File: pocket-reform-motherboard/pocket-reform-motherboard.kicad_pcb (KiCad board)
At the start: 2 copper layers, 130 x 80 mm, 20 parts, among them J1 PWR, J2 Micro_SD_Card_Det, J3 USB_C_Receptacle, J4 AudioJack4, J5 USB_C_Receptacle, J6 USBINT, J7 HDMI_D_1.4, J8 SIM, U1 reform2-som-connector, U2 MPCIE-Socket-reform-motherboa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, U3 TUSB4041I, U4 WM8960, U6 MPCIE-Socket-reform-motherboa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

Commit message: motherboard D-1 first schematic and placement
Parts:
- added BT1: V364, Battery:BatteryHolder_Keystone_2998_1x6.8mm, F.Cu at (77.0, 146.8)
- added C1: 0.1uF, Capacitor_SMD:C_0603_1608Metric, F.Cu at (86.0, 138.5)
- added C10: 1uF, Capacitor_SMD:C_0603_1608Metric, F.Cu at (89.0, 105.3)
- added C11: 10nF, Capacitor_SMD:C_0603_1608Metric, F.Cu at (119.3, 147.2)
- added C12: 10nF, Capacitor_SMD:C_0603_1608Metric, F.Cu at (137.8, 147.5)
- added C123: 47uF, Capacitor_SMD:C_0603_1608Metric, F.Cu at (190.2, 140.5)
- added C124: 47uF, Capacitor_SMD:C_0603_1608Metric, F.Cu at (148.2, 138.2)
- added C126: 47uF, Capacitor_SMD:C_0603_1608Metric, F.Cu at (148.2, 140.0)
- added C13: 12pF, Capacitor_SMD:C_0603_1608Metric, F.Cu at (167.0, 84.2)
- added C14: 68uF, Capacitor_SMD:C_0603_1608Metric, F.Cu at (101.2, 136.5)
- added C15: 330uF, Capacitor_SMD:C_0603_1608Metric, F.Cu at (111.2, 149.0)
- added C16: 330uF, Capacitor_SMD:C_0603_1608Metric, F.Cu at (129.5, 149.2)
- added C17: 10uF, Capacitor_SMD:C_0603_1608Metric, F.Cu at (161.8, 81.8)
- added C18: 10nF, Capacitor_SMD:C_0603_1608Metric, F.Cu at (113.8, 150.0)
- added C19: 10nF, Capacitor_SMD:C_0603_1608Metric, F.Cu at (132.2, 150.5)
- added C2: 4.7uF, Capacitor_SMD:C_0603_1608Metric, F.Cu at (111.0, 142.5)
- added C20: 1uF, Capacitor_SMD:C_0603_1608Metric, F.Cu at (90.8, 122.0)
- added C21: 18pF, Capacitor_SMD:C_0603_1608Metric, F.Cu at (177.6, 109.8)
- added C22: 27pF, Capacitor_SMD:C_0603_1608Metric, F.Cu at (84.8, 82.8)
- added C23: 18pF, Capacitor_SMD:C_0603_1608Metric, F.Cu at (173.3, 106.9)
- added C24: 27pF, Capacitor_SMD:C_0603_1608Metric, F.Cu at (82.1, 79.1)
- added C25: 0.1uF, Capacitor_SMD:C_0603_1608Metric, F.Cu at (75.2, 74.2)
- added C26: 1uF, Capacitor_SMD:C_0603_1608Metric, F.Cu at (68.2, 83.8)
- added C27: 0.1uF, Capacitor_SMD:C_0603_1608Metric, F.Cu at (71.6, 74.2)
- added C28: 0.1uF, Capacitor_SMD:C_0603_1608Metric, F.Cu at (68.2, 79.0)
- added C29: 0.1uF, Capacitor_SMD:C_0603_1608Metric, F.Cu at (80.8, 75.5)
- added C3: 4.7uF, Capacitor_SMD:C_0603_1608Metric, F.Cu at (129.5, 142.8)
- added C30: 0.1uF, Capacitor_SMD:C_0603_1608Metric, F.Cu at (80.8, 77.2)
- added C31: 0.1uF, Capacitor_SMD:C_0603_1608Metric, F.Cu at (75.2, 86.0)
- added C32: 0.1uF, Capacitor_SMD:C_0603_1608Metric, F.Cu at (71.2, 86.0)
- added C33: 0.1uF, Capacitor_SMD:C_0603_1608Metric, F.Cu at (68.2, 82.2)
- added C34: 1uF, Capacitor_SMD:C_0603_1608Metric, F.Cu at (68.2, 77.5)
- added C35: 0.1uF, Capacitor_SMD:C_0603_1608Metric, F.Cu at (62.0, 74.2)
- added C36: 1uF, Capacitor_SMD:C_0603_1608Metric, F.Cu at (68.2, 75.8)
- added C37: 1nF, Capacitor_SMD:C_0603_1608Metric, F.Cu at (195.5, 69.0)
- added C38: 0.1uF, Capacitor_SMD:C_0603_1608Metric, F.Cu at (80.8, 73.9)
- added C39: 10uF, Capacitor_SMD:C_0603_1608Metric, F.Cu at (170.5, 78.0)
- added C4: 4.7uF, Capacitor_SMD:C_0603_1608Metric, F.Cu at (112.8, 142.5)
- added C40: 0.1uF, Capacitor_SMD:C_0603_1608Metric, F.Cu at (68.2, 80.8)
- added C41: 0.1uF, Capacitor_SMD:C_0603_1608Metric, F.Cu at (170.5, 79.8)
- added C42: 0.1uF, Capacitor_SMD:C_0603_1608Metric, F.Cu at (188.0, 69.0)
- added C43: 0.1uF, Capacitor_SMD:C_0603_1608Metric, F.Cu at (186.5, 69.0)
- added C44: 0.1uF, Capacitor_SMD:C_0603_1608Metric, F.Cu at (185.0, 69.0)
- added C45: 0.1uF, Capacitor_SMD:C_0603_1608Metric, F.Cu at (183.5, 69.0)
- added C46: 0.1uF, Capacitor_SMD:C_0603_1608Metric, F.Cu at (80.5, 98.5)
- added C47: 0.1uF, Capacitor_SMD:C_0603_1608Metric, F.Cu at (197.0, 133.2)
- added C48: 0.1uF, Capacitor_SMD:C_0603_1608Metric, F.Cu at (159.0, 122.8)
- added C49: 0.1uF, Capacitor_SMD:C_0603_1608Metric, F.Cu at (157.9, 112.0)
- added C5: 4.7uF, Capacitor_SMD:C_0603_1608Metric, F.Cu at (131.2, 142.8)
- added C50: 0.1uF, Capacitor_SMD:C_0603_1608Metric, F.Cu at (77.5, 128.2)
- added C51: 10uF, Capacitor_SMD:C_0603_1608Metric, F.Cu at (80.7, 126.5)
- added C52: 10nF, Capacitor_SMD:C_0603_1608Metric, F.Cu at (171.2, 137.6)
- added C53: 0.1uF, Capacitor_SMD:C_0603_1608Metric, F.Cu at (171.2, 140.6)
- added C54: 0.1uF, Capacitor_SMD:C_0603_1608Metric, F.Cu at (171.2, 139.0)
- added C55: 0.1uF, Capacitor_SMD:C_0603_1608Metric, F.Cu at (175.8, 140.5)
- added C56: 10uF, Capacitor_SMD:C_0603_1608Metric, F.Cu at (69.5, 122.0)
- added C57: 0.1uF, Capacitor_SMD:C_0603_1608Metric, F.Cu at (80.5, 121.5)
- added C58: 10nF, Capacitor_SMD:C_0603_1608Metric, F.Cu at (159.0, 138.5)
- added C59: 0.1uF, Capacitor_SMD:C_0603_1608Metric, F.Cu at (162.2, 138.5)
- added C6: 4.7uF, Capacitor_SMD:C_0603_1608Metric, F.Cu at (163.0, 91.2)
- added C60: 0.1uF, Capacitor_SMD:C_0603_1608Metric, F.Cu at (162.2, 140.2)
- added C61: 0.1uF, Capacitor_SMD:C_0603_1608Metric, F.Cu at (165.5, 140.2)
- added C62: 0.1uF, Capacitor_SMD:C_0603_1608Metric, F.Cu at (71.0, 122.1)
- added C63: 0.1uF, Capacitor_SMD:C_0603_1608Metric, F.Cu at (163.2, 111.0)
- added C64: 0.1uF, Capacitor_SMD:C_0603_1608Metric, F.Cu at (162.2, 122.8)
- added C65: 10uF, Capacitor_SMD:C_0603_1608Metric, F.Cu at (191.2, 105.8)
- added C66: 0.1uF, Capacitor_SMD:C_0603_1608Metric, F.Cu at (193.0, 105.8)
- added C67: 10uF, Capacitor_SMD:C_0603_1608Metric, F.Cu at (80.0, 124.0)
- added C68: 0.1uF, Capacitor_SMD:C_0603_1608Metric, F.Cu at (74.5, 130.0)
- added C69: 0.1uF, Capacitor_SMD:C_0603_1608Metric, F.Cu at (80.0, 117.0)
- added C7: 10nF, Capacitor_SMD:C_0603_1608Metric, F.Cu at (114.5, 142.5)
- added C72: 0.1uF, Capacitor_SMD:C_0603_1608Metric, F.Cu at (199.3, 90.1)
- added C73: 0.1uF, Capacitor_SMD:C_0603_1608Metric, F.Cu at (193.0, 88.5)
- added C76: 0.1uF, Capacitor_SMD:C_0603_1608Metric, F.Cu at (69.7, 138.1)
- added C77: 0.1uF, Capacitor_SMD:C_0603_1608Metric, F.Cu at (186.8, 88.0)
- added C78: 0.1uF, Capacitor_SMD:C_0603_1608Metric, F.Cu at (65.0, 148.5)
- added C8: 10nF, Capacitor_SMD:C_0603_1608Metric, F.Cu at (133.0, 142.8)
- added C82: 470nF, Capacitor_SMD:C_0603_1608Metric, F.Cu at (68.5, 146.0)
- added C83: 47uF, Capacitor_SMD:C_0603_1608Metric, F.Cu at (187.2, 140.5)
- added C85: 0.1uF, Capacitor_SMD:C_0603_1608Metric, F.Cu at (170.2, 119.2)
- added C86: 0.1uF, Capacitor_SMD:C_0603_1608Metric, F.Cu at (170.2, 125.8)
- added C87: 0.1uF, Capacitor_SMD:C_0603_1608Metric, F.Cu at (200.2, 98.9)
- added C88: 0.1uF, Capacitor_SMD:C_0603_1608Metric, F.Cu at (168.8, 119.2)
- added C89: 0.1uF, Capacitor_SMD:C_0603_1608Metric, F.Cu at (168.8, 125.8)
- added C9: 1uF, Capacitor_SMD:C_0603_1608Metric, F.Cu at (93.4, 105.2)
- added C90: 0.1uF, Capacitor_SMD:C_0603_1608Metric, F.Cu at (178.8, 129.0)
- added C91: 0.1uF, Capacitor_SMD:C_0603_1608Metric, F.Cu at (182.5, 129.0)
- added C92: 0.1uF, Capacitor_SMD:C_0603_1608Metric, F.Cu at (177.2, 129.0)
- added C93: 0.1uF, Capacitor_SMD:C_0603_1608Metric, F.Cu at (181.0, 129.0)
- added D1: LED_MODEM, LED_SMD:LED_0603_1608Metric, F.Cu at (193.6, 149.5)
- added D10: 19-337/R6GHBHC-A01/2T, LED_SMD:LED_RGB_PLCC-6, F.Cu at (67.5, 70.1)
- added D11: SS54?, Diode_SMD:D_SMA, F.Cu at (91.8, 138.0)
- added D12: SD0603S040S0R2, Diode_SMD:D_0603_1608Metric, F.Cu at (189.8, 88.5)
- added D2: SMAJ36CA-E3/5A, Diode_SMD:D_SMA, F.Cu at (78.6, 139.8)
- added D23: LED_NVME, LED_SMD:LED_0603_1608Metric, F.Cu at (168.1, 149.5)
- added D3: BZT52C10, Diode_SMD:D_SOD-123, F.Cu at (85.5, 140.5)
- added D4: B540C, Diode_SMD:D_SMA, F.Cu at (102.8, 140.0)
- added D5: B540C, Diode_SMD:D_SMA, F.Cu at (108.5, 147.8)
- added D6: B540C, Diode_SMD:D_SMA, F.Cu at (126.8, 147.8)
- added D7: BZX84-C5V6,215, Diode_SMD:D_SOD-323, F.Cu at (88.8, 122.2)
- added D8: LED_Small, LED_SMD:LED_0603_1608Metric, F.Cu at (201.5, 68.2)
- added D9: LED_Small, LED_SMD:LED_0603_1608Metric, F.Cu at (201.5, 70.0)
- added FB1: 220@100MHz 1.4A, Inductor_SMD:L_0603_1608Metric, F.Cu at (170.5, 81.5)
- added FB10: 100@100MHz 3A, Inductor_SMD:L_0603_1608Metric, F.Cu at (73.0, 139.5)
- added FB2: 100@100MHz 3A, Inductor_SMD:L_0603_1608Metric, F.Cu at (80.5, 119.8)
- added FB3: 100@100MHz 3A, Inductor_SMD:L_0603_1608Metric, F.Cu at (171.3, 135.9)
- added FB4: 100@100MHz 3A, Inductor_SMD:L_0603_1608Metric, F.Cu at (146.5, 136.6)
- added FB5: 100@100MHz 3A, Inductor_SMD:L_0603_1608Metric, F.Cu at (76.9, 117.0)
- added FB8: 100@100MHz 3A, Inductor_SMD:L_0603_1608Metric, F.Cu at (164.8, 111.0)
- added FB9: 100@100MHz 3A, Inductor_SMD:L_0603_1608Metric, F.Cu at (71.5, 139.5)
- added H5: NGFF-Mount1, footprints:WA-SMSI-M2, F.Cu at (156.0, 87.0)
- added H6: NGFF-Mount1, footprints:WA-SMSI-M2, F.Cu at (156.0, 107.0)
- added H7: NGFF-Mount1, footprints:WA-SMSI-M2, F.Cu at (181.0, 107.0)
- added J10: 1-2199230-6, footprints:TE_1-2199230-6, F.Cu at (156.0, 145.0)
- added J11: Conn_01x33, Connector_FFC-FPC:Hirose_FH12-33S-0.5SH_1x33-1MP_P0.50mm_Horizontal, F.Cu at (64.8, 116.6)
- added J12: 2199230-5, footprints:TE_2199230-5, F.Cu at (181.0, 145.0)
- added J13: FH35C-31S-0.3HW(50), footprints:TE_3-2328724-1, F.Cu at (61.9, 133.8)
- added J14: USB_C_Receptacle, Connector_USB:USB_C_Receptacle_Amphenol_12401548E4-2A_CircularHoles, F.Cu at (204.9, 141.0)
- added J15: Conn_01x02, Connector_JST:JST_GH_SM02B-GHS-TB_1x02-1MP_P1.25mm_Horizontal, F.Cu at (63.3, 143.2)
- added J9: USB_C_Receptacle_USB2.0, Connector_USB:USB_C_Receptacle_HRO_TYPE-C-31-M-12, F.Cu at (148.7, 71.1)
- added L1: 47uH, Inductor_SMD:L_1210_3225Metric, F.Cu at (96.5, 140.0)
- added L2: 2.2uH, Inductor_SMD:L_1210_3225Metric, F.Cu at (162.0, 84.2)
- added L3: 15uH, Inductor_SMD:L_1210_3225Metric, F.Cu at (113.8, 146.8)
- added L4: 15uH, Inductor_SMD:L_1210_3225Metric, F.Cu at (132.2, 147.3)
- added L5: 15uH, Inductor_SMD:L_1210_3225Metric, F.Cu at (68.6, 142.3)
- added L6: 15uH, Inductor_SMD:L_1210_3225Metric, F.Cu at (68.3, 148.7)
- added MK1: MP23ABS1TR, footprints:MIC_MP23ABS1TR, F.Cu at (97.7, 68.9)
- added Q1: Si7461DP, footprints:PowerPAK_SO-8_Single_8Pads, F.Cu at (85.2, 133.8)
- added R1: 1k, Resistor_SMD:R_0603_1608Metric, F.Cu at (195.5, 149.5)
- added R10: 200k, Resistor_SMD:R_0603_1608Metric, F.Cu at (167.8, 87.8)
- added R100: 47k, Resistor_SMD:R_0603_1608Metric, F.Cu at (116.1, 70.0)
- added R101: 0, Resistor_SMD:R_0603_1608Metric, F.Cu at (181.6, 137.2)
- added R102: 0, Resistor_SMD:R_0603_1608Metric, F.Cu at (181.6, 135.7)
- added R103: 0, Resistor_SMD:R_0603_1608Metric, F.Cu at (187.2, 138.5)
- added R104: 0, Resistor_SMD:R_0603_1608Metric, F.Cu at (161.7, 134.5)
- added R105: 0, Resistor_SMD:R_0603_1608Metric, F.Cu at (158.1, 134.5)
- added R106: 0, Resistor_SMD:R_0603_1608Metric, F.Cu at (154.6, 134.5)
- added R107: 0, Resistor_SMD:R_0603_1608Metric, F.Cu at (163.2, 134.5)
- added R108: 0, Resistor_SMD:R_0603_1608Metric, F.Cu at (159.6, 134.5)
- added R109: 0, Resistor_SMD:R_0603_1608Metric, F.Cu at (156.1, 134.5)
- added R11: 0, Resistor_SMD:R_0603_1608Metric, F.Cu at (126.4, 96.9)
- added R110: 1k, Resistor_SMD:R_0603_1608Metric, F.Cu at (168.1, 143.5)
- added R111: 0, Resistor_SMD:R_0603_1608Metric, F.Cu at (190.2, 138.5)
- added R12: 0, Resistor_SMD:R_0603_1608Metric, F.Cu at (87.8, 82.3)
- added R13: 0, Resistor_SMD:R_0603_1608Metric, F.Cu at (87.8, 84.0)
- added R14: 280k, Resistor_SMD:R_0603_1608Metric, F.Cu at (165.5, 84.2)
- added R15: 10k, Resistor_SMD:R_0603_1608Metric, F.Cu at (124.0, 145.5)
- added R16: 3.16k, Resistor_SMD:R_0603_1608Metric, F.Cu at (124.0, 142.2)
- added R17: 10k, Resistor_SMD:R_0603_1608Metric, F.Cu at (142.5, 145.4)
- added R18: 5.83k, Resistor_SMD:R_0603_1608Metric, F.Cu at (142.5, 142.1)
- added R19: 1.3M, Resistor_SMD:R_0603_1608Metric, F.Cu at (97.2, 122.8)
- added R198: 49.9, Resistor_SMD:R_0603_1608Metric, F.Cu at (126.8, 116.0)
- added R199: 49.9, Resistor_SMD:R_0603_1608Metric, F.Cu at (126.8, 114.5)
- added R2: 62, Resistor_SMD:R_0603_1608Metric, F.Cu at (80.7, 136.7)
- added R20: 300k, Resistor_SMD:R_0603_1608Metric, F.Cu at (98.9, 122.9)
- added R21: 1M, Resistor_SMD:R_0603_1608Metric, F.Cu at (90.8, 125.2)
- added R22: 10k, Resistor_SMD:R_0603_1608Metric, F.Cu at (172.5, 129.0)
- added R23: DNP, Resistor_SMD:R_0603_1608Metric, F.Cu at (174.0, 129.0)
- added R24: 4.7k, Resistor_SMD:R_0603_1608Metric, F.Cu at (187.0, 120.2)
- added R25: 4.7k, Resistor_SMD:R_0603_1608Metric, F.Cu at (187.8, 122.8)
- added R26: 4.7k, Resistor_SMD:R_0603_1608Metric, F.Cu at (188.8, 120.2)
- added R27: 200k, Resistor_SMD:R_0603_1608Metric, F.Cu at (175.5, 129.0)
- added R28: 120k, Resistor_SMD:R_0603_1608Metric, F.Cu at (93.5, 125.5)
- added R29: 1k, Resistor_SMD:R_0603_1608Metric, F.Cu at (198.2, 68.3)
- added R3: 1M, Resistor_SMD:R_0603_1608Metric, F.Cu at (89.0, 136.0)
- added R30: 10k, Resistor_SMD:R_0603_1608Metric, F.Cu at (186.0, 110.2)
- added R31: 36k, Resistor_SMD:R_0603_1608Metric, F.Cu at (186.0, 107.2)
- added R32: 10k, Resistor_SMD:R_0603_1608Metric, F.Cu at (186.0, 108.8)
- added R33: 36k, Resistor_SMD:R_0603_1608Metric, F.Cu at (186.0, 105.8)
- added R34: 1k, Resistor_SMD:R_0603_1608Metric, F.Cu at (198.2, 70.0)
- added R35: 1k, Resistor_SMD:R_0603_1608Metric, F.Cu at (79.6, 80.7)
- added R36: 1k, Resistor_SMD:R_0603_1608Metric, F.Cu at (63.1, 86.3)
- added R37: 75 1%, Resistor_SMD:R_0603_1608Metric, F.Cu at (189.5, 69.0)
- added R38: 10k, Resistor_SMD:R_0603_1608Metric, F.Cu at (61.6, 86.4)
- added R39: 75 1%, Resistor_SMD:R_0603_1608Metric, F.Cu at (191.0, 69.0)
- added R4: 0, Resistor_SMD:R_0603_1608Metric, F.Cu at (96.0, 103.2)
- added R40: 75 1%, Resistor_SMD:R_0603_1608Metric, F.Cu at (192.5, 69.0)
- added R41: 75 1%, Resistor_SMD:R_0603_1608Metric, F.Cu at (194.0, 69.0)
- added R44: 0, Resistor_SMD:R_0603_1608Metric, F.Cu at (81.8, 86.2)
- added R45: 0, Resistor_SMD:R_0603_1608Metric, F.Cu at (86.8, 77.2)
- added R46: 0, Resistor_SMD:R_0603_1608Metric, F.Cu at (77.0, 90.2)
- added R47: 27.4, Resistor_SMD:R_0603_1608Metric, F.Cu at (92.1, 78.6)
- added R48: 27.4, Resistor_SMD:R_0603_1608Metric, F.Cu at (92.1, 80.2)
- added R49: 0, Resistor_SMD:R_0603_1608Metric, F.Cu at (77.0, 91.8)
- added R5: 0, Resistor_SMD:R_0603_1608Metric, F.Cu at (142.7, 88.1)
- added R50: 0, Resistor_SMD:R_0603_1608Metric, F.Cu at (81.8, 88.0)
- added R51: 0, Resistor_SMD:R_0603_1608Metric, F.Cu at (77.0, 93.2)
- added R52: 10k, Resistor_SMD:R_0603_1608Metric, F.Cu at (182.6, 111.3)
- added R53: 12k 1%, Resistor_SMD:R_0603_1608Metric, F.Cu at (170.8, 109.4)
- added R54: 10k, Resistor_SMD:R_0603_1608Metric, F.Cu at (170.8, 113.0)
- added R55: 200k, Resistor_SMD:R_0603_1608Metric, F.Cu at (187.0, 115.5)
- added R56: 10k, Resistor_SMD:R_0603_1608Metric, F.Cu at (65.0, 97.5)
- added R57: 4.7k, Resistor_SMD:R_0603_1608Metric, F.Cu at (69.2, 87.5)
- added R58: 1k, Resistor_SMD:R_0603_1608Metric, F.Cu at (71.8, 68.3)
- added R59: 4.7k, Resistor_SMD:R_0603_1608Metric, F.Cu at (67.5, 87.5)
- added R6: 100k, Resistor_SMD:R_0603_1608Metric, F.Cu at (117.0, 137.2)
- added R60: 1k, Resistor_SMD:R_0603_1608Metric, F.Cu at (71.9, 70.1)
- added R61: 1k, Resistor_SMD:R_0603_1608Metric, F.Cu at (71.9, 71.7)
- added R62: DNP, Resistor_SMD:R_0603_1608Metric, F.Cu at (152.1, 77.3)
- added R63: DNP, Resistor_SMD:R_0603_1608Metric, F.Cu at (147.5, 78.2)
- added R64: DNP, Resistor_SMD:R_0603_1608Metric, F.Cu at (149.2, 78.2)
- added R65: 49.9, Resistor_SMD:R_0603_1608Metric, F.Cu at (126.8, 111.5)
- added R66: 49.9, Resistor_SMD:R_0603_1608Metric, F.Cu at (126.8, 113.0)
- added R67: 0, Resistor_SMD:R_0603_1608Metric, F.Cu at (126.4, 89.8)
- added R68: 10k, Resistor_SMD:R_0603_1608Metric, F.Cu at (194.8, 130.8)
- added R69: 100k, Resistor_SMD:R_0603_1608Metric, F.Cu at (72.0, 115.0)
- added R7: 100k, Resistor_SMD:R_0603_1608Metric, F.Cu at (117.0, 135.5)
- added R70: 0, Resistor_SMD:R_0603_1608Metric, F.Cu at (73.0, 117.7)
- added R71: 0, Resistor_SMD:R_0603_1608Metric, F.Cu at (71.0, 125.5)
- added R72: 2k2, Resistor_SMD:R_0603_1608Metric, F.Cu at (74.5, 128.5)
- added R75: 10k, Resistor_SMD:R_0603_1608Metric, F.Cu at (164.8, 122.0)
- added R76: 33, Resistor_SMD:R_0603_1608Metric, F.Cu at (108.0, 119.7)
- added R77: 33, Resistor_SMD:R_0603_1608Metric, F.Cu at (106.3, 124.8)
- added R79: 33, Resistor_SMD:R_0603_1608Metric, F.Cu at (112.0, 123.2)
- added R8: 100k, Resistor_SMD:R_0603_1608Metric, F.Cu at (167.2, 90.2)
- added R80: 33, Resistor_SMD:R_0603_1608Metric, F.Cu at (126.6, 81.1)
- added R81: 0, Resistor_SMD:R_0603_1608Metric, F.Cu at (160.0, 110.2)
- added R82: 33, Resistor_SMD:R_0603_1608Metric, F.Cu at (126.5, 79.5)
- added R83: 0, Resistor_SMD:R_0603_1608Metric, F.Cu at (169.6, 123.2)
- added R84: 0, Resistor_SMD:R_0603_1608Metric, F.Cu at (169.6, 121.7)
- added R85: 10k, Resistor_SMD:R_0603_1608Metric, F.Cu at (187.8, 90.5)
- added R87: 100k, Resistor_SMD:R_0603_1608Metric, F.Cu at (126.7, 127.6)
- added R89: 4.7k, Resistor_SMD:R_0603_1608Metric, F.Cu at (201.8, 88.5)
- added R9: 0, Resistor_SMD:R_0603_1608Metric, F.Cu at (98.2, 133.0)
- added R90: 27k, Resistor_SMD:R_0603_1608Metric, F.Cu at (197.5, 87.8)
- added R93: 4.7k, Resistor_SMD:R_0603_1608Metric, F.Cu at (201.8, 87.0)
- added R96: 10k, Resistor_SMD:R_0603_1608Metric, F.Cu at (207.2, 87.8)
- added R97: 47k, Resistor_SMD:R_0603_1608Metric, F.Cu at (116.1, 68.5)
- added R98: 47k, Resistor_SMD:R_0603_1608Metric, F.Cu at (116.1, 71.5)
- added R99: 47k, Resistor_SMD:R_0603_1608Metric, F.Cu at (116.1, 72.9)
- added SW1: SW_DIP_x01, Button_Switch_SMD:SW_DIP_SPSTx01_Slide_Omron_A6S-110x_W8.9mm_P2.54mm, F.Cu at (61.4, 93.4)
- added SW2: RESET, Button_Switch_SMD:SW_Push_1P1T_NO_CK_KMR2, F.Cu at (61.2, 102.0)
- added TP3: PRTCTL2, TestPoint:TestPoint_Pad_D1.0mm, F.Cu at (188.8, 126.8)
- added TP4: PRTCTL4, TestPoint:TestPoint_Pad_D1.0mm, F.Cu at (186.6, 129.9)
- added TP5: TestPoint, TestPoint:TestPoint_Pad_D1.0mm, F.Cu at (80.1, 69.8)
- added TP6: TestPoint, TestPoint:TestPoint_Pad_D1.0mm, F.Cu at (82.8, 69.8)
- added TR1: TG111-MSC13LF, Transformer_SMD:Transformer_Ethernet_HALO_TG111-MSC13, F.Cu at (188.8, 78.4)
- added U10: W25Q32JVSS, Package_SO:SOIC-8_5.23x5.23mm_P1.27mm, F.Cu at (63.4, 80.0)
- added U11: PCF8523T, Package_SO:SOIC-8_3.9x4.9mm_P1.27mm, F.Cu at (75.8, 99.5)
- added U12: AP22815, Package_TO_SOT_SMD:SOT-23-5, F.Cu at (194.0, 133.3)
- added U13: TXS0108EPW, Package_SO:TSSOP-20_4.4x6.5mm_P0.65mm, F.Cu at (161.5, 116.5)
- added U14: SN74AVC1T45, Package_TO_SOT_SMD:SOT-23-6, F.Cu at (161.7, 125.5)
- added U15: TPD4E02B04DQA, Package_SON:USON-10_2.5x1.0mm_P0.5mm, F.Cu at (195.5, 141.2)
- added U16: TPD4E02B04DQA, Package_SON:USON-10_2.5x1.0mm_P0.5mm, F.Cu at (195.5, 124.0)
- added U17: TPD12S521, footprints:TSSOP50P640X120-38N, F.Cu at (193.7, 94.8)
- added U18: TLV320AIC3100, Package_DFN_QFN:VQFN-32-1EP_5x5mm_P0.5mm_EP3.5x3.5mm, F.Cu at (75.3, 123.3)
- added U19: TPD4E02B04DQA, Package_SON:USON-10_2.5x1.0mm_P0.5mm, F.Cu at (195.5, 144.5)
- added U20: TPD4E02B04DQA, Package_SON:USON-10_2.5x1.0mm_P0.5mm, F.Cu at (195.5, 127.5)
- added U21: TPD4E02B04DQA, Package_SON:USON-10_2.5x1.0mm_P0.5mm, F.Cu at (195.5, 138.0)
- added U22: TPD4E02B04DQA, Package_SON:USON-10_2.5x1.0mm_P0.5mm, F.Cu at (195.5, 120.5)
- added U23: FUSB302BMPX, Package_DFN_QFN:WQFN-14-1EP_2.5x2.5mm_P0.5mm_EP1.45x1.45mm, F.Cu at (149.5, 131.7)
- added U5: TPS5450DDAR, Package_SO:TI_SO-PowerPAD-8_ThermalVias, F.Cu at (119.2, 143.5)
- added U7: CN301, Package_TO_SOT_SMD:SOT-23-5, F.Cu at (94.0, 122.8)
- added U8: RP2040, footprints:RP2040-QFN-56, F.Cu at (74.4, 80.1)
- added U9: USB7002/KDX, footprints:QFN40P1200X1200X90-101N, F.Cu at (179.2, 119.4)
- added Y1: 25MHz, Crystal:Crystal_SMD_Abracon_ABM8G-4Pin_3.2x2.5mm, F.Cu at (174.5, 109.7)
- added Y2: 12MHz 18pF, Crystal:Crystal_SMD_3225-4Pin_3.2x2.5mm, F.Cu at (82.1, 82.2)
- added Y3: 32.768 kHz, Crystal:Crystal_SMD_3215-2Pin_3.2x1.5mm, F.Cu at (70.4, 98.8)
- J1: value PWR -> CHARGER; footprint Connector_JST:JST_PH_S4B-PH-SM4-TB_1x04-1MP_P2.00mm_Horizontal -> Connector_JST:JST_PH_S9B-PH-SM4-TB_1x09-1MP_P2.00mm_Horizontal
- J4: value AudioJack4 -> 09452812561; footprint Connector_Audio:Jack_3.5mm_CUI_SJ-3524-SMT_Horizontal -> footprints:09452812561
- J5: value USB_C_Receptacle -> SYSCTL; footprint Connector_USB:USB_C_Receptacle_Amphenol_12401548E4-2A_CircularHoles -> Connector_JST:JST_PH_S4B-PH-SM4-TB_1x04-1MP_P2.00mm_Horizontal
- J6: value USBINT -> USB_INT1
- J8: value SIM -> SIM_Card; footprint footprints:TE_2199337-5 -> footprints:MOLEX_78800-0001
- TP1: value TestPoint_2Pole -> PRTCTL1; footprint footprints:MOLEX_48099-5701 -> TestPoint:TestPoint_Pad_D1.0mm
- TP2: value TestPoint_2Pole -> PRTCTL3; footprint footprints:MOLEX_48099-5701 -> TestPoint:TestPoint_Pad_D1.0mm
- U2: value MPCIE-Socket-reform-motherboard-rescue -> MAX1837EUT33+T; footprint footprints:MOLEX_67910-5700 -> Package_TO_SOT_SMD:SOT-23-6
- U3: value TUSB4041I -> LM3674MFX-ADJ/NOPB; footprint Package_QFP:HTQFP-64-1EP_10x10mm_P0.5mm_EP8x8mm_Mask4.4x4.4mm_ThermalVias -> Package_TO_SOT_SMD:SOT-23-5
- U4: value WM8960 -> TLV1117-18; footprint Package_DFN_QFN:QFN-32-1EP_5x5mm_P0.5mm_EP3.3x3.3mm -> Package_TO_SOT_SMD:SOT-223
- U6: value MPCIE-Socket-reform-motherboard-rescue -> TPS5450DDAR; footprint footprints:MOLEX_67910-5700 -> Package_SO:TI_SO-PowerPAD-8_ThermalVias
- moved J2 97.5 mm to (201.5, 108.8), turned to 90 degrees
- moved U4 95.5 mm to (90.5, 99.8), turned to 90 degrees
- moved J1 70.5 mm to (94.8, 147.0), turned to 0 degrees
- moved J7 63.0 mm to (207.0, 94.8), turned to 90 degrees
- moved U2 62.6 mm to (98.7, 136.0), turned to -90 degrees
- moved J3 52.1 mm to (205.0, 124.0), turned to 90 degrees
- moved J8 49.6 mm to (177.5, 95.0), turned to -90 degrees
- moved GFX1 33.9 mm to (146.8, 106.8), turned to 90 degrees
- moved TP2 29.6 mm to (188.7, 128.9), turned to 0 degrees
- moved H1 20.6 mm to (62.0, 70.0)
- moved H2 20.0 mm to (62.0, 149.0)
- moved TP1 18.5 mm to (186.7, 127.7), turned to 0 degrees
- moved J6 16.6 mm to (174.5, 72.0)
- moved U6 16.5 mm to (137.8, 143.8), turned to 180 degrees
- moved U1 13.3 mm to (135.0, 104.0)
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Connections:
- net Net-(U1-Pad122) renamed IMX_UART2_RX
- net Net-(U1-Pad124) renamed IMX_UART2_TX
- net Net-(U1-Pad126) renamed IMX_UART1_RX
- net Net-(U1-Pad128) renamed IMX_UART1_TX
- net Net-(U1-Pad164) renamed BACKLIGHT_PWM
- net Net-(U1-Pad168) renamed DAC_RXFS
- net Net-(U1-Pad87) renamed IMX_RESETn
- J1 pad 1: +5V -> Net-(J1-Pad1)
- J1 pad 2: +5V -> Net-(J1-Pad1)
- J1 pad 3: GND -> VCHG
- J1 pad 4: GND -> VCHG
- J2 pad 1: SD_D2 -> Net-(J2-Pad1)
- J2 pad 2: SD_D3 -> Net-(J2-Pad2)
- J2 pad 3: SD_CMD -> Net-(J2-Pad3)
- J2 pad 5: SD_CLK -> Net-(J2-Pad5)
- J2 pad 6: Net-(J2-Pad6) -> GND
- J2 pad 7: SD_D0 -> Net-(J2-Pad7)
- J2 pad 8: SD_D1 -> Net-(J2-Pad8)
- J2 pad 9: Net-(J2-Pad9) -> SD_DET
- J3 pad A1: Net-(J3-PadA1) -> GND
- J3 pad A10: USB2_RXN -> USBH_1B_RXN
- J3 pad A11: USB2_RXP -> USBH_1B_RXP
- J3 pad A12: Net-(J3-PadA1) -> GND
- J3 pad A2: USB2_TXP -> Net-(J3-PadA2)
- J3 pad A3: USB2_TXN -> Net-(J3-PadA3)
- J3 pad A4: Net-(J3-PadA4) -> +5V
- J3 pad A6: USB12_DP -> USBH_1_DP
- J3 pad A7: USB12_DN -> USBH_1_DN
- J3 pad A8: Net-(J3-PadA8) -> unconnected-(J3-PadA8)
- J3 pad A9: Net-(J3-PadA4) -> +5V
- J3 pad B1: Net-(J3-PadA1) -> GND
- J3 pad B10: USB2_RXN -> USBH_1A_RXN
- J3 pad B11: USB2_RXP -> USBH_1A_RXP
- J3 pad B12: Net-(J3-PadA1) -> GND
- J3 pad B2: USB2_TXP -> Net-(J3-PadB2)
- J3 pad B3: USB2_TXN -> Net-(J3-PadB3)
- J3 pad B4: Net-(J3-PadA4) -> +5V
- J3 pad B6: USB12_DP -> USBH_1_DP
- J3 pad B7: USB12_DN -> USBH_1_DN
- J3 pad B8: Net-(J3-PadB8) -> unconnected-(J3-PadB8)
- J3 pad B9: Net-(J3-PadA4) -> +5V
- J3 pad S1: Net-(J3-PadS1) -> GND
- J6 pad 2: USB13_DP -> USBH_3_DN
- J6 pad 3: USB13_DN -> USBH_3_DP
- J6 pad 4: Net-(J6-Pad4) -> GND
- J7 pad 10: Net-(J7-Pad10) -> GND
- J7 pad 13: Net-(J7-Pad13) -> GND
- J7 pad 16: Net-(J7-Pad16) -> GND
- J7 pad 2: Net-(J7-Pad2) -> unconnected-(J7-Pad2)
- J7 pad 4: Net-(J7-Pad4) -> GND
- J7 pad 7: Net-(J7-Pad7) -> GND
- J7 pad SH: Net-(J7-PadSH) -> GND
- J8 pad 1: Net-(J8-Pad1) -> UIM_PWR
- J8 pad 5: Net-(J8-Pad5) -> GND
- TP1 pad 1: GND -> /PRT_CTL1
- TP2 pad 1: GND -> /PRT_CTL3
- U1 pad 10: Net-(U1-Pad10) -> unconnected-(U1-Pad10)
- U1 pad 101: Net-(U1-Pad101) -> DAC_SCL
- U1 pad 103: Net-(U1-Pad103) -> DAC_SDA
- U1 pad 104: Net-(U1-Pad104) -> GND
- U1 pad 105: Net-(U1-Pad105) -> unconnected-(U1-Pad105)
- U1 pad 107: Net-(U1-Pad107) -> unconnected-(U1-Pad107)
- U1 pad 109: Net-(U1-Pad109) -> unconnected-(U1-Pad109)
- U1 pad 11: Net-(U1-Pad11) -> ETH0_D+
- U1 pad 110: Net-(U1-Pad110) -> GND
- U1 pad 111: Net-(U1-Pad111) -> unconnected-(U1-Pad111)
- U1 pad 116: Net-(U1-Pad116) -> GND
- U1 pad 117: Net-(U1-Pad117) -> unconnected-(U1-Pad117)
- U1 pad 120: Net-(U1-Pad120) -> unconnected-(U1-Pad120)
- U1 pad 123: Net-(U1-Pad123) -> unconnected-(U1-Pad123)
- U1 pad 129: Net-(U1-Pad129) -> GND
- U1 pad 13: Net-(U1-Pad13) -> GND
- U1 pad 130: Net-(U1-Pad130) -> unconnected-(U1-Pad130)
- U1 pad 131: Net-(U1-Pad131) -> ~{USBH_RESET}
- U1 pad 132: Net-(U1-Pad132) -> unconnected-(U1-Pad132)
- U1 pad 133: Net-(U1-Pad133) -> unconnected-(U1-Pad133)
- U1 pad 134: Net-(U1-Pad134) -> unconnected-(U1-Pad134)
- U1 pad 135: Net-(U1-Pad135) -> unconnected-(U1-Pad135)
- U1 pad 136: Net-(U1-Pad136) -> unconnected-(U1-Pad136)
- U1 pad 137: Net-(U1-Pad137) -> unconnected-(U1-Pad137)
- U1 pad 138: Net-(U1-Pad138) -> unconnected-(U1-Pad138)
- U1 pad 139: Net-(U1-Pad139) -> unconnected-(U1-Pad139)
- U1 pad 140: Net-(U1-Pad140) -> unconnected-(U1-Pad140)
- U1 pad 141: Net-(U1-Pad141) -> IMX_RTC_IRQ
- U1 pad 142: Net-(U1-Pad142) -> unconnected-(U1-Pad142)
- U1 pad 143: Net-(U1-Pad143) -> unconnected-(U1-Pad143)
- U1 pad 144: Net-(U1-Pad144) -> unconnected-(U1-Pad144)
- U1 pad 145: Net-(U1-Pad145) -> IMX_WAKE
- U1 pad 146: Net-(U1-Pad146) -> unconnected-(U1-Pad146)
- U1 pad 147: Net-(U1-Pad147) -> unconnected-(U1-Pad147)
- U1 pad 148: Net-(U1-Pad148) -> unconnected-(U1-Pad148)
- U1 pad 149: Net-(U1-Pad149) -> unconnected-(U1-Pad149)
- U1 pad 15: Net-(U1-Pad15) -> ETH0_C-
- U1 pad 150: Net-(U1-Pad150) -> unconnected-(U1-Pad150)
- U1 pad 151: Net-(U1-Pad151) -> unconnected-(U1-Pad151)
- U1 pad 152: Net-(U1-Pad152) -> unconnected-(U1-Pad152)
- U1 pad 153: Net-(U1-Pad153) -> unconnected-(U1-Pad153)
- U1 pad 154: Net-(U1-Pad154) -> unconnected-(U1-Pad154)
- U1 pad 155: Net-(U1-Pad155) -> unconnected-(U1-Pad155)
- U1 pad 156: Net-(U1-Pad156) -> unconnected-(U1-Pad156)
- U1 pad 157: Net-(U1-Pad157) -> unconnected-(U1-Pad157)
- U1 pad 158: Net-(U1-Pad158) -> unconnected-(U1-Pad158)
- U1 pad 159: Net-(U1-Pad159) -> unconnected-(U1-Pad159)
- U1 pad 160: Net-(U1-Pad160) -> unconnected-(U1-Pad160)
- U1 pad 161: Net-(U1-Pad161) -> GND
- U1 pad 162: Net-(U1-Pad162) -> unconnected-(U1-Pad162)
- U1 pad 166: Net-(U1-Pad166) -> DAC_DIN
- U1 pad 167: Net-(U1-Pad167) -> GND
- U1 pad 17: Net-(U1-Pad17) -> ETH0_C+
- U1 pad 170: Net-(U1-Pad170) -> DAC_BCLK
- U1 pad 172: Net-(U1-Pad172) -> DAC_TXFS
- U1 pad 173: Net-(U1-Pad173) -> GND
- U1 pad 174: Net-(U1-Pad174) -> unconnected-(U1-Pad174)
- U1 pad 176: Net-(U1-Pad176) -> DAC_MCLK
- U1 pad 178: Net-(U1-Pad178) -> DAC_DOUT
- U1 pad 179: Net-(U1-Pad179) -> GND
- U1 pad 180: Net-(U1-Pad180) -> unconnected-(U1-Pad180)
- U1 pad 182: Net-(U1-Pad182) -> unconnected-(U1-Pad182)
- U1 pad 184: Net-(U1-Pad184) -> unconnected-(U1-Pad184)
- U1 pad 185: Net-(U1-Pad185) -> GND
- U1 pad 186: Net-(U1-Pad186) -> unconnected-(U1-Pad186)
- U1 pad 188: Net-(U1-Pad188) -> unconnected-(U1-Pad188)
- U1 pad 19: Net-(U1-Pad19) -> GND
- U1 pad 190: Net-(U1-Pad190) -> unconnected-(U1-Pad190)
- U1 pad 191: Net-(U1-Pad191) -> GND
- U1 pad 192: Net-(U1-Pad192) -> unconnected-(U1-Pad192)
- U1 pad 193: Net-(U1-Pad193) -> HDMI_SDA
- U1 pad 194: Net-(U1-Pad194) -> unconnected-(U1-Pad194)
- U1 pad 195: Net-(U1-Pad195) -> HDMI_SCL
- U1 pad 196: Net-(U1-Pad196) -> unconnected-(U1-Pad196)
- U1 pad 197: Net-(U1-Pad197) -> HDMI_CEC
- U1 pad 198: Net-(U1-Pad198) -> unconnected-(U1-Pad198)
- U1 pad 199: Net-(U1-Pad199) -> HDMI_HPD
- U1 pad 200: Net-(U1-Pad200) -> unconnected-(U1-Pad200)
- U1 pad 21: Net-(U1-Pad21) -> ETH0_B-
- U1 pad 23: Net-(U1-Pad23) -> ETH0_B+
- U1 pad 24: Net-(U1-Pad24) -> PCIE2_RESETn
- U1 pad 25: Net-(U1-Pad25) -> GND
- U1 pad 26: Net-(U1-Pad26) -> SD_DET
- U1 pad 27: Net-(U1-Pad27) -> ETH0_A-
- U1 pad 28: Net-(U1-Pad28) -> unconnected-(U1-Pad28)
- U1 pad 29: Net-(U1-Pad29) -> ETH0_A+
- U1 pad 31: Net-(U1-Pad31) -> GND
- U1 pad 33: Net-(U1-Pad33) -> unconnected-(U1-Pad33)
- U1 pad 34: Net-(U1-Pad34) -> unconnected-(U1-Pad34)
- U1 pad 35: Net-(U1-Pad35) -> unconnected-(U1-Pad35)
- U1 pad 36: Net-(U1-Pad36) -> unconnected-(U1-Pad36)
- U1 pad 37: Net-(U1-Pad37) -> PCIE1_RESETn
- U1 pad 38: Net-(U1-Pad38) -> unconnected-(U1-Pad38)
- U1 pad 39: Net-(U1-Pad39) -> unconnected-(U1-Pad39)
- U1 pad 40: Net-(U1-Pad40) -> unconnected-(U1-Pad40)
- U1 pad 41: Net-(U1-Pad41) -> GND
- U1 pad 42: Net-(U1-Pad42) -> unconnected-(U1-Pad42)
- U1 pad 43: Net-(U1-Pad43) -> unconnected-(U1-Pad43)
- U1 pad 44: Net-(U1-Pad44) -> GND
- U1 pad 45: Net-(U1-Pad45) -> unconnected-(U1-Pad45)
- U1 pad 47: Net-(U1-Pad47) -> GND
- U1 pad 49: Net-(U1-Pad49) -> unconnected-(U1-Pad49)
- U1 pad 50: Net-(U1-Pad50) -> GND
- U1 pad 51: Net-(U1-Pad51) -> unconnected-(U1-Pad51)
- U1 pad 53: Net-(U1-Pad53) -> GND
- U1 pad 55: Net-(U1-Pad55) -> unconnected-(U1-Pad55)
- U1 pad 56: Net-(U1-Pad56) -> GND
- U1 pad 57: Net-(U1-Pad57) -> unconnected-(U1-Pad57)
- U1 pad 58: Net-(U1-Pad58) -> PCIE1_CLK_P
- U1 pad 59: Net-(U1-Pad59) -> GND
- U1 pad 60: Net-(U1-Pad60) -> PCIE1_CLK_N
- U1 pad 61: Net-(U1-Pad61) -> unconnected-(U1-Pad61)
- U1 pad 62: Net-(U1-Pad62) -> GND
- U1 pad 63: Net-(U1-Pad63) -> unconnected-(U1-Pad63)
- U1 pad 64: Net-(U1-Pad64) -> PCIE2_CLK_P
- U1 pad 65: Net-(U1-Pad65) -> GND
- U1 pad 66: Net-(U1-Pad66) -> PCIE2_CLK_N
- U1 pad 67: Net-(U1-Pad67) -> unconnected-(U1-Pad67)
- U1 pad 68: Net-(U1-Pad68) -> GND
- U1 pad 69: Net-(U1-Pad69) -> unconnected-(U1-Pad69)
- U1 pad 7: Net-(U1-Pad7) -> GND
- U1 pad 70: Net-(U1-Pad70) -> PCIE2_TX_P
- U1 pad 71: Net-(U1-Pad71) -> GND
- U1 pad 72: Net-(U1-Pad72) -> PCIE2_TX_N
- U1 pad 73: Net-(U1-Pad73) -> unconnected-(U1-Pad73)
- U1 pad 74: Net-(U1-Pad74) -> GND
- U1 pad 75: Net-(U1-Pad75) -> unconnected-(U1-Pad75)
- U1 pad 76: Net-(U1-Pad76) -> PCIE2_RX_P
- U1 pad 77: Net-(U1-Pad77) -> unconnected-(U1-Pad77)
- U1 pad 78: Net-(U1-Pad78) -> PCIE2_RX_N
- U1 pad 79: Net-(U1-Pad79) -> ETH0_LED_RX
- U1 pad 8: Net-(U1-Pad8) -> unconnected-(U1-Pad8)
- U1 pad 80: Net-(U1-Pad80) -> GND
- U1 pad 81: Net-(U1-Pad81) -> unconnected-(U1-Pad81)
- U1 pad 82: Net-(U1-Pad82) -> unconnected-(U1-Pad82)
- U1 pad 83: Net-(U1-Pad83) -> ETH0_LED_LINK1
- U1 pad 84: Net-(U1-Pad84) -> unconnected-(U1-Pad84)
- U1 pad 85: Net-(U1-Pad85) -> unconnected-(U1-Pad85)
- U1 pad 86: Net-(U1-Pad86) -> unconnected-(U1-Pad86)
- U1 pad 88: Net-(U1-Pad88) -> unconnected-(U1-Pad88)
- U1 pad 89: Net-(U1-Pad89) -> LPC_SS0
- U1 pad 9: Net-(U1-Pad9) -> ETH0_D-
- U1 pad 90: Net-(U1-Pad90) -> unconnected-(U1-Pad90)
- U1 pad 91: Net-(U1-Pad91) -> LPC_MOSI
- U1 pad 92: Net-(U1-Pad92) -> unconnected-(U1-Pad92)
- U1 pad 93: Net-(U1-Pad93) -> LPC_MISO
- U1 pad 94: Net-(U1-Pad94) -> GND
- U1 pad 95: Net-(U1-Pad95) -> unconnected-(U1-Pad95)
- U1 pad 96: Net-(U1-Pad96) -> unconnected-(U1-Pad96)
- U1 pad 97: Net-(U1-Pad97) -> LPC_SCK
- U1 pad 98: Net-(U1-Pad98) -> GND
- U1 pad 99: Net-(U1-Pad99) -> unconnected-(U1-Pad99)
- U2 pad 2: Net-(U2-Pad2) -> GND
- U2 pad 3: Net-(U2-Pad3) -> VCC
- U2 pad 5: Net-(U2-Pad5) -> ~{STANDBY_SHDN}
- U2 pad 6: Net-(U2-Pad6) -> STANDBY_3V3
- U3 pad 1: Net-(U3-Pad1) -> +3V3
- U3 pad 2: +3V3 -> GND
- U3 pad 3: Net-(U3-Pad3) -> 1V2_ENABLE
- U4 pad 1: Net-(U4-Pad1) -> GND
- U4 pad 2: Net-(U4-Pad2) -> +1V8
- U4 pad 4: Net-(U4-Pad4) -> (no net)
- U6 pad 2: Net-(U6-Pad2) -> unconnected-(U6-Pad2)
- U6 pad 3: Net-(U6-Pad3) -> unconnected-(U6-Pad3)
- U6 pad 5: Net-(U6-Pad5) -> 3V3_ENABLE
- U6 pad 6: Net-(U6-Pad6) -> GND
- U6 pad 7: Net-(U6-Pad7) -> VCC
- U6 pad 9: Net-(U6-Pad9) -> GND
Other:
- board size 130 x 80 mm -> 150 x 85 mm
- net class Default removed

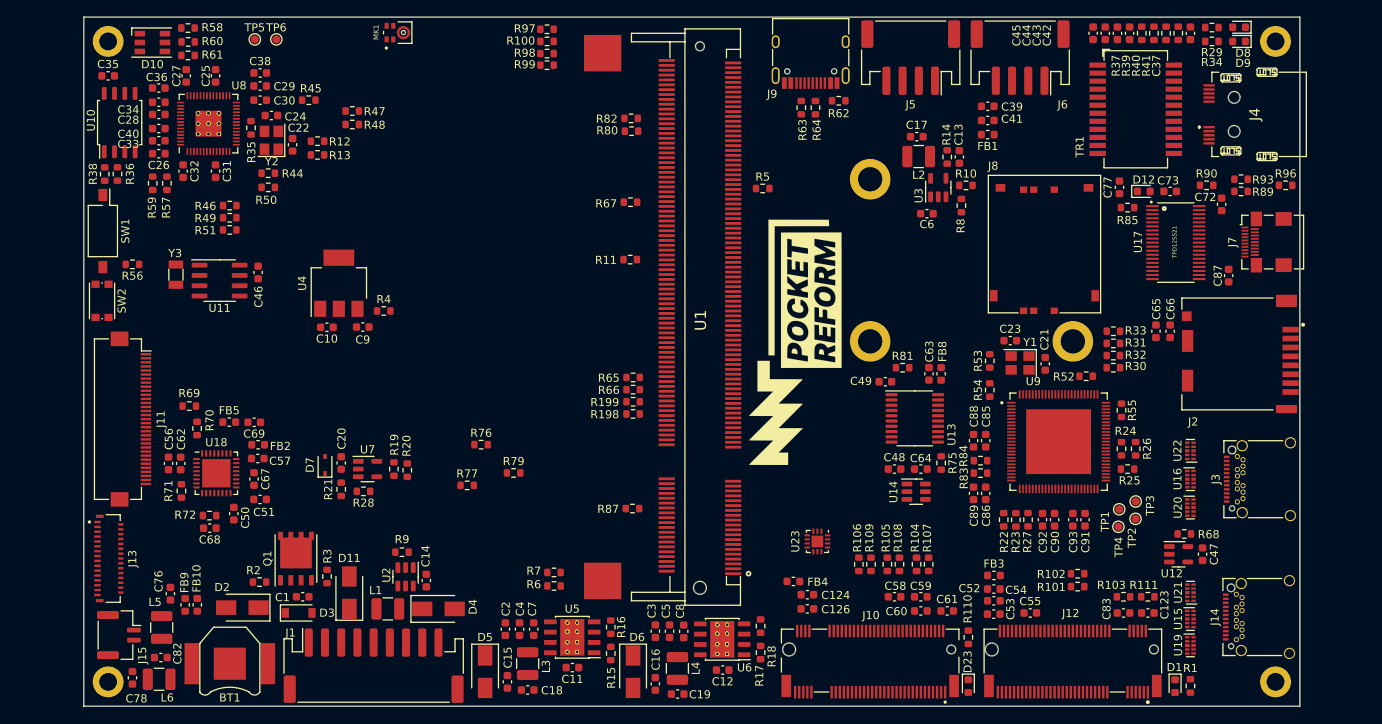
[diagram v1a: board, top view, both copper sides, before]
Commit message: motherboard: first routing
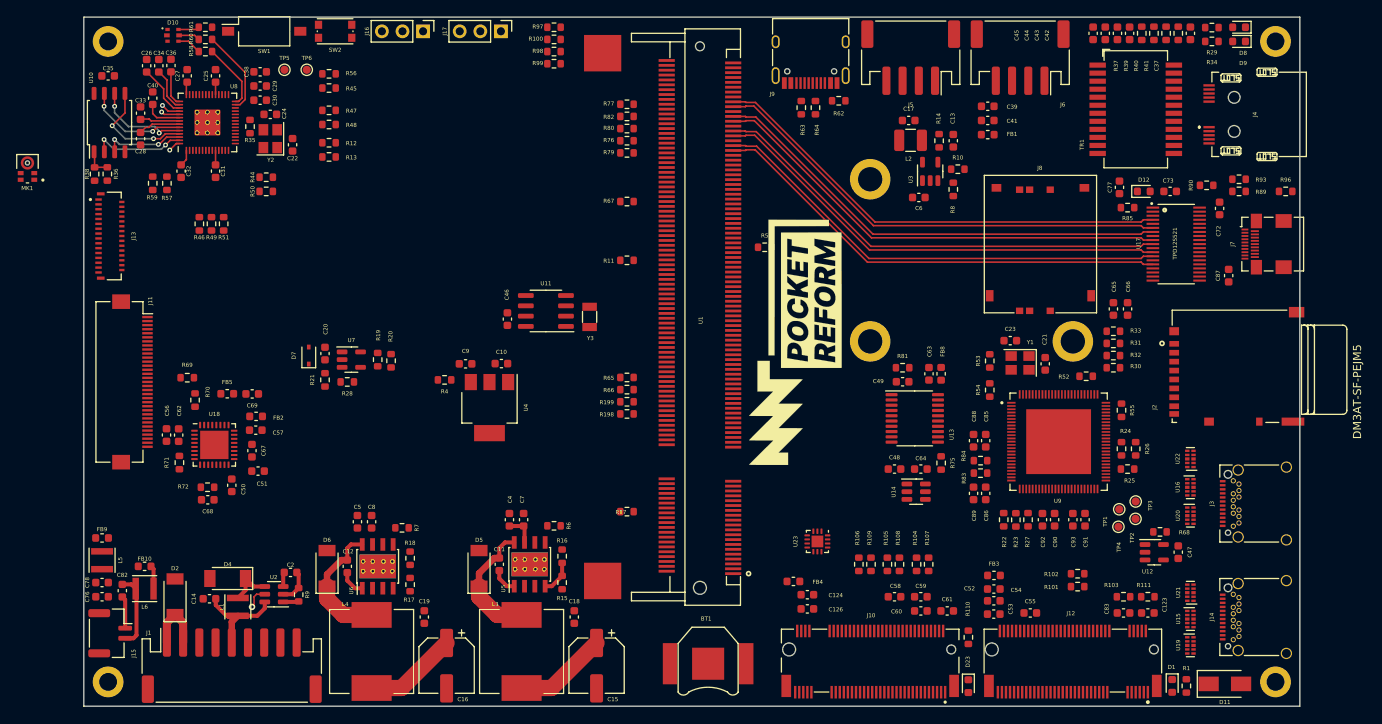
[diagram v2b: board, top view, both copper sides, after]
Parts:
- removed C1: 0.1uF, Capacitor_SMD:C_0603_1608Metric
- removed C3: 4.7uF, Capacitor_SMD:C_0603_1608Metric
- removed D3: BZT52C10, Diode_SMD:D_SOD-123
- removed Q1: Si7461DP, footprints:PowerPAK_SO-8_Single_8Pads
- removed R2: 62, Resistor_SMD:R_0603_1608Metric
- removed R3: 1M, Resistor_SMD:R_0603_1608Metric
- added J16: Conn_01x03, Connector_PinHeader_2.54mm:PinHeader_1x03_P2.54mm_Vertical, F.Cu at (100.8, 68.8)
- added J17: Conn_01x03, Connector_PinHeader_2.54mm:PinHeader_1x03_P2.54mm_Vertical, F.Cu at (110.5, 68.8)
- C14: value 68uF -> 47uF
- C15, C16: footprint Capacitor_SMD:C_0603_1608Metric -> Capacitor_SMD:CP_Elec_6.3x5.4
- C2, C4, C5, C6: value 4.7uF -> 10uF
- D10: footprint LED_SMD:LED_RGB_PLCC-6 -> footprints:LED_19-337_R6GHBHC-A01_2T
- D2: value SMAJ36CA-E3/5A -> PMEG3050EP,115; footprint Diode_SMD:D_SMA -> Diode_SMD:D_SOD-128
- D4, D5, D6: value B540C -> PMEG3050EP,115; footprint Diode_SMD:D_SMA -> Diode_SMD:D_SOD-128
- J2: value Micro_SD_Card_Det -> DM3AT-SF-PEJM5; footprint footprints:HRS_DM3CS-SF -> footprints:DM3AT-SF-PEJM5
- L1: value 47uH -> 22uH; footprint Inductor_SMD:L_1210_3225Metric -> Inductor_SMD:L_Taiyo-Yuden_NR-30xx
- L3, L4: footprint Inductor_SMD:L_1210_3225Metric -> Inductor_SMD:L_Vishay_IHLP-4040
- L5, L6: footprint Inductor_SMD:L_1210_3225Metric -> Inductor_SMD:L_Taiyo-Yuden_NR-30xx
- moved D11 108.6 mm to (199.8, 149.2), turned to 0 degrees
- moved BT1 59.0 mm to (136.0, 146.8)
- moved Y3 51.3 mm to (121.4, 104.0), turned to -90 degrees
- moved R77 51.0 mm to (126.0, 77.8), turned to 180 degrees
- moved MK1 48.7 mm to (52.0, 85.7), turned to 180 degrees
- moved C12 48.0 mm to (91.5, 134.8), turned to 90 degrees
- moved R17 44.0 mm to (99.2, 137.0)
- moved R18 44.0 mm to (99.2, 133.8)
- moved SW2 44.0 mm to (90.0, 68.8), turned to 0 degrees
- moved U6 43.4 mm to (95.2, 134.8), turned to 90 degrees
- moved R79 41.9 mm to (126.0, 83.8), turned to 180 degrees
- moved R76 41.6 mm to (126.0, 82.2), turned to 180 degrees
- moved C8 40.8 mm to (94.5, 129.2)
- moved C5 40.8 mm to (92.8, 129.2)
- moved U11 40.4 mm to (116.0, 103.2), turned to 180 degrees
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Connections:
- D2 pad 1: Net-(J1-Pad1) -> VCC
- J1 pad 1: Net-(J1-Pad1) -> VCC
- J1 pad 2: Net-(J1-Pad1) -> VCC
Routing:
- net HDMI_TX2P: track 0.00 -> 58.0 mm
- net HDMI_TX2N: track 0.00 -> 58.0 mm
- net HDMI_TX1P: track 0.00 -> 57.9 mm
- net HDMI_TX1N: track 0.00 -> 57.9 mm
- net HDMI_TX0P: track 0.00 -> 57.8 mm
- net HDMI_TX0N: track 0.00 -> 57.8 mm
- net HDMI_CLKP: track 0.00 -> 57.7 mm
- net HDMI_CLKN: track 0.00 -> 57.7 mm
- net STANDBY_3V3: track 0.00 -> 33.8 mm
- net Net-(C11-Pad2): track 0.00 -> 16.5 mm
- net +5V: track 0.00 -> 16.2 mm
- net Net-(C12-Pad2): track 0.00 -> 16.1 mm
- net QSPI_SD0: track 0.00 -> 13.9 mm, vias 0 -> 2
- net VCC: track 0.00 -> 13.3 mm
- net QSPI_SD3: track 0.00 -> 12.7 mm, vias 0 -> 2
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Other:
- copper layers 2 -> 6
- board text added: "11mm overmold"
- board text added: "12.85mm min. distance according to spec"
